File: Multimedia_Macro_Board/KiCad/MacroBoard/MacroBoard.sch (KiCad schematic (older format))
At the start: 54 parts, among them J1 USB_C_Receptacle_USB2.0, SW1 SW_Push, SW10 SW_MEC_5G, SW11 SW_MEC_5G, SW12 SW_MEC_5G, SW13 SW_MEC_5G, SW14 SW_MEC_5G, SW15 SW_MEC_5G, SW16 SW_MEC_5G, SW17 SW_MEC_5G, SW18 SW_MEC_5G, SW19 SW_MEC_5G, SW2 SW_MEC_5G, SW20 SW_MEC_5G, SW21 SW_MEC_5G, SW22 SW_MEC_5G, SW23 Rotary_Encoder, SW3 SW_MEC_5G, SW4 SW_MEC_5G, SW5 SW_MEC_5G, SW6 SW_MEC_5G, SW7 SW_MEC_5G, SW8 SW_MEC_5G, SW9 SW_MEC_5G, U1 ATmega32U4-MU

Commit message: finished schematic
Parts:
- removed Y?: Crystal_GND2, symbol Device:Crystal_GND2
- added C1, C2: 22pF, symbol Device:C
- added C10, C9: 10nF, symbol Device:C
- added C4, C5, C6, C7: 100nF, symbol Device:C
- added C8: 10uF, symbol Device:C
- added J2: AVR-ISP-6, symbol Connector:AVR-ISP-6
- added R10, R7, R8, R9: 10k, symbol Device:R
- added Y1: Crystal_GND24_16MHz, symbol Device:Crystal_GND24
- renumbered C1 to C3
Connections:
- net GND: now also SW23.C, C1.2, C10.2, C2.2, C4.2, C5.2, C6.2, C7.2, C8.2, C9.1, J2.6 (GND), Y1.2, Y1.4
- net REA: now also C10.1, R10.1
- net REB: now also C9.2, R9.2
- net Row1: now also J2.3 (SCK)
- net VCC: now also C4.1, C5.1, C6.1, C7.1, C8.1, J2.2 (VCC), R7.2, R8.1
- net XTAL1: now also C1.1, Y1.1
- net XTAL2: now also C2.1, Y1.3
- net RST: now reaches R1.1, SW1.2, U1.13 (~RESET)
- net RST: now also J2.5 (~RST)
- net at SW23.A: now also R10.2, R8.2
- net at SW23.B: now also R7.1, R9.1
- net Row2 renamed MOSI
- net MOSI: now also J2.4 (MOSI)
- net Row3 renamed MISO
- net MISO: now also J2.1 (MISO)
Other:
- note added: "10uF for VCC, remainder for Vin"
- note added: "C1=C2=2(CL-Cstray)"
- note removed: "May need filter here"
- note removed: "Needs xtal and load capacitors"
- note removed: "VCC mat need filter"
- moved on the sheet: R1, SW23

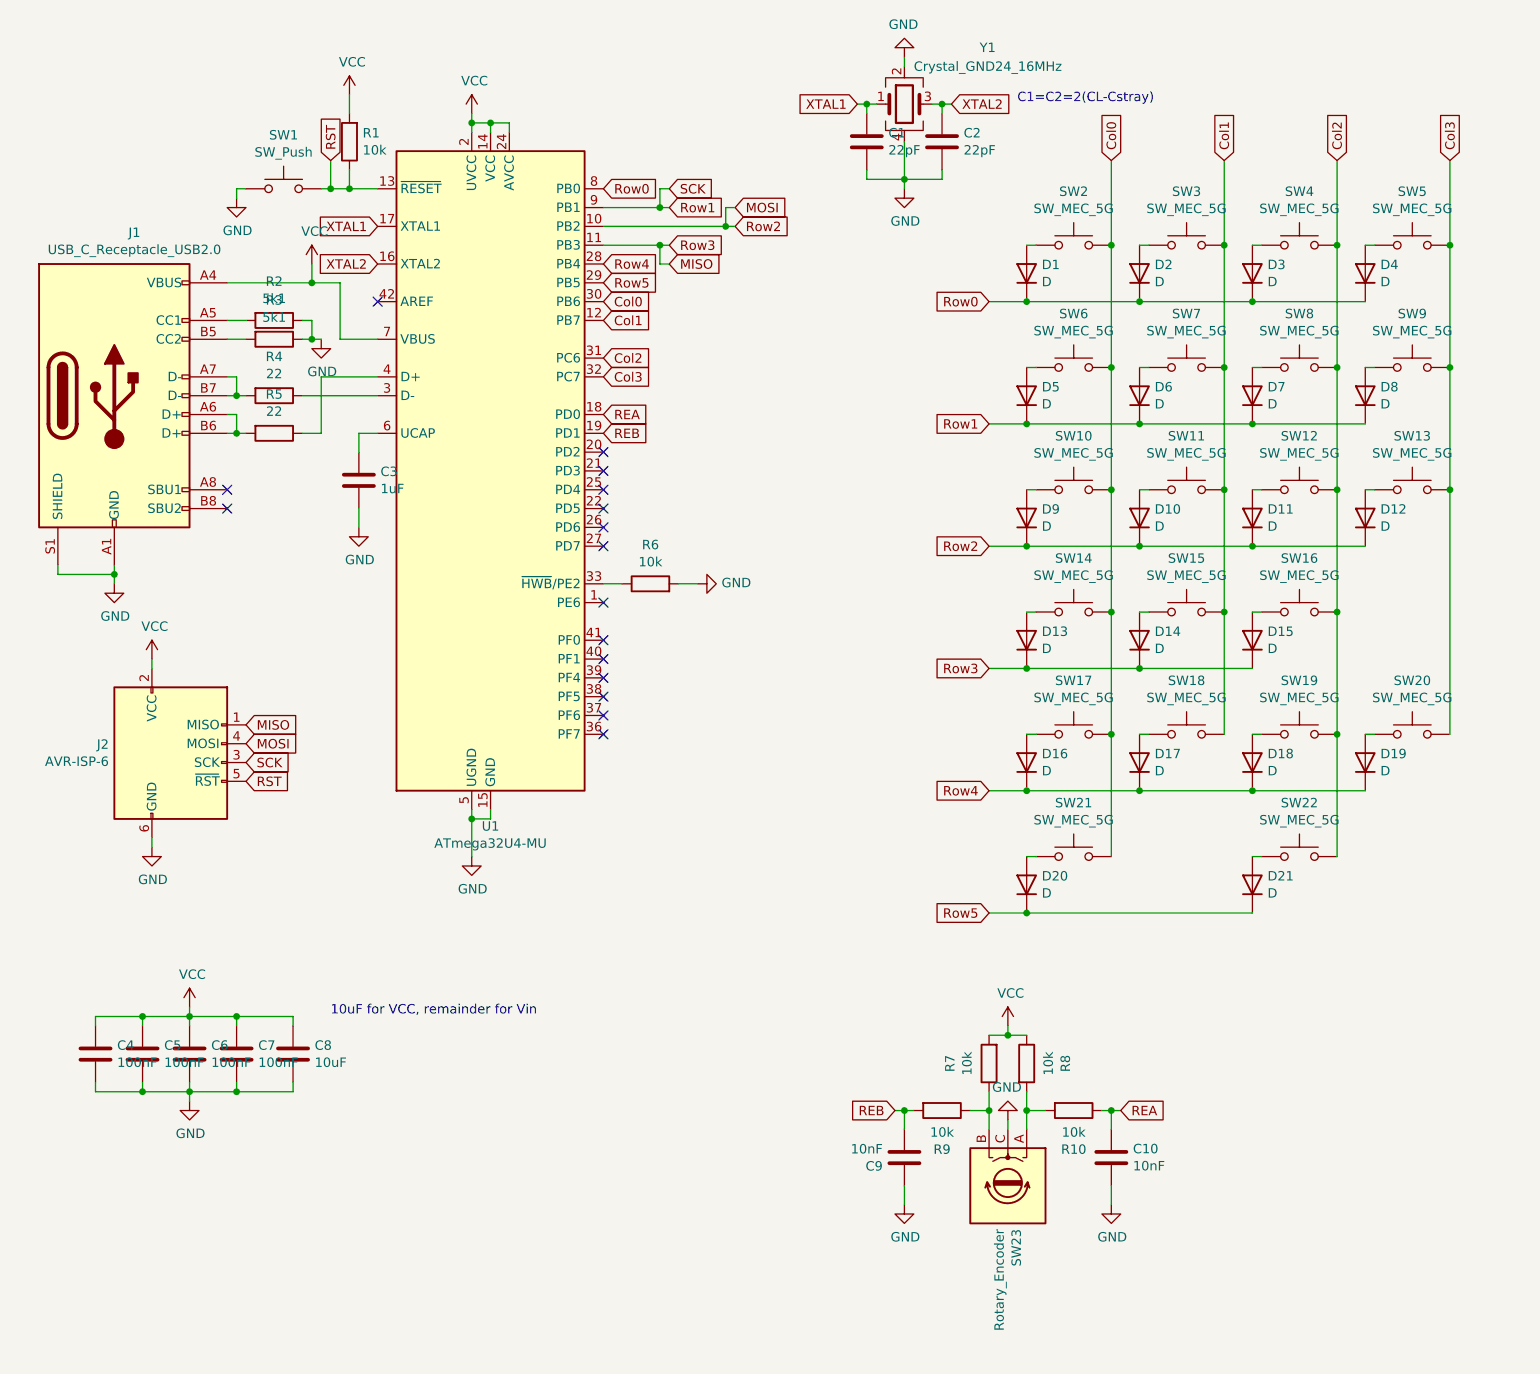
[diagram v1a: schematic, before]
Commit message: Created pcb file
To do:
-borders
-numlock LED
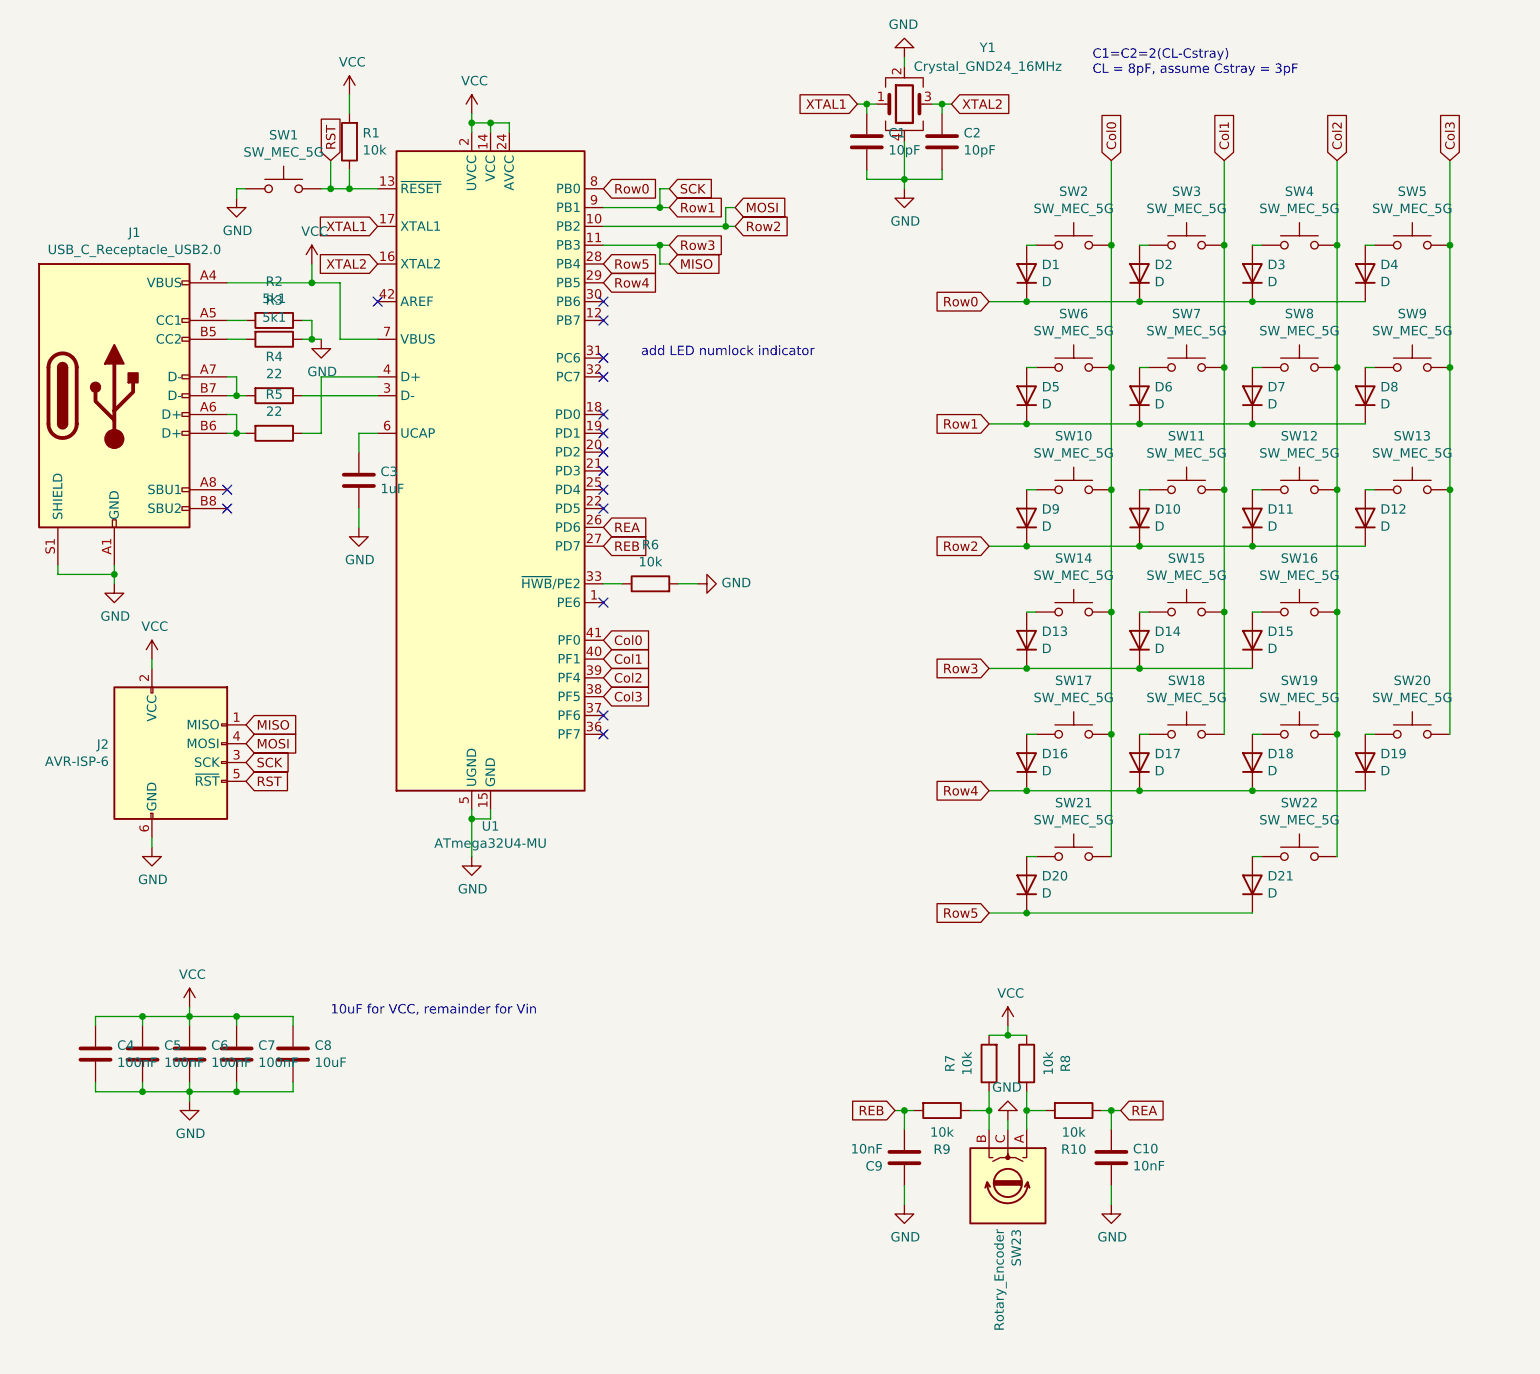
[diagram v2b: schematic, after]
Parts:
- removed SW1: SW_Push, symbol Switch:SW_Push
- removed SW10, SW11, SW12, SW14, SW15, SW16, SW17, SW18, SW19, SW2, SW22, SW3, SW4, SW5, SW6, SW7, SW8, SW9: SW_MEC_5G, Button_Switch_Keyboard:SW_Cherry_MX_1.00u_PCB, symbol Switch:SW_MEC_5G
- removed SW13, SW20: SW_MEC_5G, Button_Switch_Keyboard:SW_Cherry_MX_2.00u_Vertical_PCB, symbol Switch:SW_MEC_5G
- removed SW21: SW_MEC_5G, Button_Switch_Keyboard:SW_Cherry_MX_2.00u_PCB, symbol Switch:SW_MEC_5G
- added SW1: SW_MEC_5G, MacroBoard:Button_Breakout, symbol keyboard:SW_MEC_5G
- added SW10, SW11, SW12, SW14, SW15, SW16, SW17, SW18, SW19, SW2, SW22, SW3, SW4, SW5, SW6, SW7, SW8, SW9: SW_MEC_5G, Button_Switch_Keyboard:SW_Cherry_MX_1.00u_PCB, symbol keyboard:SW_MEC_5G
- added SW13, SW20: SW_MEC_5G, Button_Switch_Keyboard:SW_Cherry_MX_2.00u_Vertical_PCB, symbol keyboard:SW_MEC_5G
- added SW21: SW_MEC_5G, Button_Switch_Keyboard:SW_Cherry_MX_2.00u_PCB, symbol keyboard:SW_MEC_5G
- C1, C2: value 22pF -> 10pF; footprint (none) -> Capacitor_SMD:C_0603_1608Metric_Pad1.08x0.95mm_HandSolder
- C10, C3, C9: footprint (none) -> Capacitor_SMD:C_0603_1608Metric_Pad1.08x0.95mm_HandSolder
- C4, C5, C6, C7: footprint (none) -> Capacitor_SMD:C_0402_1005Metric_Pad0.74x0.62mm_HandSolder
- C8: footprint (none) -> Capacitor_SMD:C_0805_2012Metric_Pad1.18x1.45mm_HandSolder
- D1, D10, D11, D12, D13, D14, D15, D16, D17, D18, D19, D2, D20, D21, D3, D4, D5, D6, D7, D8, D9: footprint (none) -> Diode_SMD:D_0603_1608Metric_Pad1.05x0.95mm_HandSolder
- J1: footprint (none) -> MacroBoard:USB4085-GF-A
- J2: footprint (none) -> MacroBoard:ISP
- R1, R10, R2, R3, R4, R5, R6, R7, R8, R9: footprint (none) -> Resistor_THT:R_Axial_DIN0207_L6.3mm_D2.5mm_P7.62mm_Horizontal
- SW23: footprint (none) -> MacroBoard:Rotary_Encoder
- Y1: footprint (none) -> MacroBoard:FA-20H_Crystal
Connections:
- net Col0: now also U1.41 (PF0), SW10.1 (A), SW10.3 (A), SW14.1 (A), SW14.3 (A), SW17.1 (A), SW17.3 (A), SW2.1 (A), SW2.3 (A), SW21.1 (A), SW21.3 (A), SW6.1 (A), SW6.3 (A); no longer U1.30 (PB6)
- net Col1: now also U1.40 (PF1), SW11.1 (A), SW11.3 (A), SW15.1 (A), SW15.3 (A), SW18.1 (A), SW18.3 (A), SW3.1 (A), SW3.3 (A), SW7.1 (A), SW7.3 (A); no longer U1.12 (PB7)
- net Col2: now also U1.39 (PF4), SW12.1 (A), SW12.3 (A), SW16.1 (A), SW16.3 (A), SW19.1 (A), SW19.3 (A), SW22.1 (A), SW22.3 (A), SW4.1 (A), SW4.3 (A), SW8.1 (A), SW8.3 (A); no longer U1.31 (PC6)
- net Col3: now also U1.38 (PF5), SW13.1 (A), SW13.3 (A), SW20.1 (A), SW20.3 (A), SW5.1 (A), SW5.3 (A), SW9.1 (A), SW9.3 (A); no longer U1.32 (PC7)
- net GND: now also SW1.2 (B), SW1.4 (B)
- net REA: now also U1.26 (PD6); no longer U1.18 (PD0)
- net REB: now also U1.27 (PD7); no longer U1.19 (PD1)
- net RST: now also SW1.1 (A), SW1.3 (A)
- net Row4: now also U1.29 (PB5); no longer U1.28 (PB4)
- net Row5: now also U1.28 (PB4); no longer U1.29 (PB5)
- net at D9.2 (A): now also SW10.2 (B), SW10.4 (B)
- net at D10.2 (A): now also SW11.2 (B), SW11.4 (B)
- net at D13.2 (A): now also SW14.2 (B), SW14.4 (B)
- net at D14.2 (A): now also SW15.2 (B), SW15.4 (B)
- net at D16.2 (A): now also SW17.2 (B), SW17.4 (B)
- net at D17.2 (A): now also SW18.2 (B), SW18.4 (B)
- net at D15.2 (A): now also SW16.2 (B), SW16.4 (B)
- net at D11.2 (A): now also SW12.2 (B), SW12.4 (B)
- net at D18.2 (A): now also SW19.2 (B), SW19.4 (B)
- net at D20.2 (A): now also SW21.2 (B), SW21.4 (B)
- net at D19.2 (A): now also SW20.2 (B), SW20.4 (B)
- net at D21.2 (A): now also SW22.2 (B), SW22.4 (B)
- net at D12.2 (A): now also SW13.2 (B), SW13.4 (B)
- net at D5.2 (A): now also SW6.2 (B), SW6.4 (B)
- net at D6.2 (A): now also SW7.2 (B), SW7.4 (B)
- net at D7.2 (A): now also SW8.2 (B), SW8.4 (B)
- net at D8.2 (A): now also SW9.2 (B), SW9.4 (B)
- net at D1.2 (A): now also SW2.2 (B), SW2.4 (B)
- net at D2.2 (A): now also SW3.2 (B), SW3.4 (B)
- net at D3.2 (A): now also SW4.2 (B), SW4.4 (B)
- net at D4.2 (A): now also SW5.2 (B), SW5.4 (B)
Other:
- note added: "C1=C2=2(CL-Cstray)\nCL = 8pF, assume Cstray = 3pF"
- note added: "add LED numlock indicator"
- note removed: "C1=C2=2(CL-Cstray)"
